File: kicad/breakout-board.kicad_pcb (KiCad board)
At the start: 2 copper layers, 15 parts, among them IC1 ATMEGA328-P, P1 CONN_01X02, P2 Conn_3, P3 Conn_2b, P4 Conn_1, P5 Conn_5, P6 Conn_6, P7 Conn_4, P8 Conn_2b, P9 6Pin Connector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

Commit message: kicad with jumper, flatcam gcode
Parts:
- added JP1: JUMPER, Resistors_ThroughHole:Resistor_Vertical_RM5mm, F.Cu at (28.2, 23.6)
- added JP2: JUMPER, Resistors_ThroughHole:Resistor_Vertical_RM5mm, F.Cu at (38.4, 16.8)
- added JP3: JUMPER, Resistors_ThroughHole:Resistor_Horizontal_RM10mm, F.Cu at (20.8, 16.5)
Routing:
- net +5V: track 46.0 -> 81.3 mm
- net GND: track 2.56 -> 0.00 mm
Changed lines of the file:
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@@
 (kicad_pcb (version 4) (host pcbnew 4.0.0-1rc2.201511201506+6189~38~ubuntu15.04.1-stable)
   (general
-    (links 44)
-    (no_connects 2)
-    (area 0 0 0 0)
+    (links 50)
+    (no_connects 3)
+    (area 11.938 11.390279 55.244 77.884001)
     (thickness 1.6)
-    (drawings 0)
-    (tracks 70)
+    (drawings 2)
+    (tracks 77)
     (zones 0)
-    (modules 15)
+    (modules 18)
     (nets 27)
   )
@@
     (pad_drill 0.6)
     (pad_to_mask_clearance 0)
-    (aux_axis_origin 0 0)
+    (aux_axis_origin 39.624 69.85)
     (visible_elements FFFFFF7F)
     (pcbplotparams
-      (layerselection 0x00030_80000001)
+      (layerselection 0x00000_00000001)
       (usegerberextensions false)
       (excludeedgelayer true)
-      (linewidth 0.100000)
+      (linewidth 0.300000)
       (plotframeref false)
       (viasonmask false)
@@
       (outputformat 1)
       (mirror false)
-      (drillshape 1)
+      (drillshape 0)
       (scaleselection 1)
       (outputdirectory ""))
@@
       (net 4 XTAL2))
   )
-  (segment (start 20.828 18.796) (end 13.97 18.796) (width 0.5) (layer F.Cu) (net 1) (status 400000))
-  (segment (start 14.478 44.45) (end 19.812 44.45) (width 0.5) (layer F.Cu) (net 1) (status 800000))
+  (module Resistors_ThroughHole:Resistor_Vertical_RM5mm (layer F.Cu)
+    (at 28.194 23.622 135)
+    (descr "Resistor, Vertical, RM 5mm, 1/3W,")
+    (tags "Resistor, Vertical, RM 5mm, 1/3W,")
+    (fp_text reference JP1 (at 2.70002 -3.29946 135) (layer F.SilkS)
+      (effects (font (size 1 1) (thickness 0.15)))
+    )
+    (fp_text value JUMPER (at 0 4.50088 135) (layer F.Fab)
+      (effects (font (size 1 1) (thickness 0.15)))
+    )
+    (fp_line (start -0.09906 0) (end 0.9017 0) (layer F.SilkS) (width 0.15))
+    (fp_circle (center -2.49936 0) (end 0 0) (layer F.SilkS) (width 0.15))
+    (pad 1 thru_hole circle (at -2.49936 0 135) (size 1.99898 1.99898) (drill 1.00076) (layers *.Cu *.SilkS *.Mask)
+      (net 2 GND))
+    (pad 2 thru_hole circle (at 2.5019 0 135) (size 1.99898 1.99898) (drill 1.00076) (layers *.Cu *.SilkS *.Mask)
+      (net 2 GND))
+  )
+  (module Resistors_ThroughHole:Resistor_Vertical_RM5mm (layer F.Cu)
+    (at 38.354 16.764 270)
+    (descr "Resistor, Vertical, RM 5mm, 1/3W,")
+    (tags "Resistor, Vertical, RM 5mm, 1/3W,")
+    (fp_text reference JP2 (at 2.70002 -3.29946 270) (layer F.SilkS)
+      (effects (font (size 1 1) (thickness 0.15)))
+    )
+    (fp_text value JUMPER (at 0 4.50088 270) (layer F.Fab)
+      (effects (font (size 1 1) (thickness 0.15)))
+    )
+    (fp_line (start -0.09906 0) (end 0.9017 0) (layer F.SilkS) (width 0.15))
+    (fp_circle (center -2.49936 0) (end 0 0) (layer F.SilkS) (width 0.15))
+    (pad 1 thru_hole circle (at -2.49936 0 180) (size 1.99898 1.99898) (drill 1.00076) (layers *.Cu *.SilkS *.Mask)
+      (net 1 +5V))
+    (pad 2 thru_hole circle (at 2.5019 0 315) (size 1.99898 1.99898) (drill 1.00076) (layers *.Cu *.SilkS *.Mask)
+      (net 1 +5V))
+  )
+  (module Resistors_ThroughHole:Resistor_Horizontal_RM10mm (layer F.Cu)
+    (at 20.828 16.51)
+    (descr "Resistor, Axial,  RM 10mm, 1/3W,")
+    (tags "Resistor, Axial, RM 10mm, 1/3W,")
+    (fp_text reference JP3 (at 0.24892 -3.50012) (layer F.SilkS)
+      (effects (font (size 1 1) (thickness 0.15)))
+    )
+    (fp_text value JUMPER (at 3.81 3.81) (layer F.Fab)
+      (effects (font (size 1 1) (thickness 0.15)))
+    )
+    (fp_line (start -2.54 -1.27) (end 2.54 -1.27) (layer F.SilkS) (width 0.15))
+    (fp_line (start 2.54 -1.27) (end 2.54 1.27) (layer F.SilkS) (width 0.15))
+    (fp_line (start 2.54 1.27) (end -2.54 1.27) (layer F.SilkS) (width 0.15))
+    (fp_line (start -2.54 1.27) (end -2.54 -1.27) (layer F.SilkS) (width 0.15))
+    (fp_line (start -2.54 0) (end -3.81 0) (layer F.SilkS) (width 0.15))
+    (fp_line (start 2.54 0) (end 3.81 0) (layer F.SilkS) (width 0.15))
+    (pad 1 thru_hole circle (at -5.08 0) (size 1.99898 1.99898) (drill 1.00076) (layers *.Cu *.SilkS *.Mask)
+      (net 2 GND))
+    (pad 2 thru_hole circle (at 5.08 0) (size 1.99898 1.99898) (drill 1.00076) (layers *.Cu *.SilkS *.Mask)
+      (net 2 GND))
+    (model Resistors_ThroughHole.3dshapes/Resistor_Horizontal_RM10mm.wrl
+      (at (xyz 0 0 0))
+      (scale (xyz 0.4 0.4 0.4))
+      (rotate (xyz 0 0 0))
+    )
+  )
+  (dimension 59.436 (width 0.3) (layer F.SilkS)
+    (gr_text "59,436 mm" (at 48.594 42.418 270) (layer F.SilkS)
+      (effects (font (size 1.5 1.5) (thickness 0.3)))
+    )
+    (feature1 (pts (xy 42.418 72.136) (xy 49.944 72.136)))
+    (feature2 (pts (xy 42.418 12.7) (xy 49.944 12.7)))
+    (crossbar (pts (xy 47.244 12.7) (xy 47.244 72.136)))
+    (arrow1a (pts (xy 47.244 72.136) (xy 46.657579 71.009496)))
+    (arrow1b (pts (xy 47.244 72.136) (xy 47.830421 71.009496)))
+    (arrow2a (pts (xy 47.244 12.7) (xy 46.657579 13.826504)))
+    (arrow2b (pts (xy 47.244 12.7) (xy 47.830421 13.826504)))
+  )
+  (dimension 30.48 (width 0.3) (layer F.SilkS)
+    (gr_text "30,480 mm" (at 27.178 76.534) (layer F.SilkS)
+      (effects (font (size 1.5 1.5) (thickness 0.3)))
+    )
+    (feature1 (pts (xy 42.418 72.136) (xy 42.418 77.884)))
+    (feature2 (pts (xy 11.938 72.136) (xy 11.938 77.884)))
+    (crossbar (pts (xy 11.938 75.184) (xy 42.418 75.184)))
+    (arrow1a (pts (xy 42.418 75.184) (xy 41.291496 75.770421)))
+    (arrow1b (pts (xy 42.418 75.184) (xy 41.291496 74.597579)))
+    (arrow2a (pts (xy 11.938 75.184) (xy 13.064504 75.770421)))
+    (arrow2b (pts (xy 11.938 75.184) (xy 13.064504 74.597579)))
+  )
+  (segment (start 35.306 18.796) (end 37.8841 18.796) (width 0.5) (layer F.Cu) (net 1))
+  (segment (start 37.8841 18.796) (end 38.354 19.2659) (width 0.5) (layer F.Cu) (net 1))
+  (segment (start 20.828 18.796) (end 20.828 14.986) (width 0.5) (layer F.Cu) (net 1))
+  (segment (start 21.54936 14.26464) (end 38.354 14.26464) (width 0.5) (layer F.Cu) (net 1))
+  (segment (start 20.828 14.986) (end 21.54936 14.26464) (width 0.5) (layer F.Cu) (net 1))
+  (segment (start 37.8841 18.796) (end 38.354 19.2659) (width 0.5) (layer F.Cu) (net 1))
+  (segment (start 22.352 44.45) (end 24.13 44.45) (width 0.5) (layer F.Cu) (net 1))
+  (segment (start 24.13 44.45) (end 29.21 49.53) (width 0.5) (layer F.Cu) (net 1))
+  (segment (start 29.21 49.53) (end 29.972 49.53) (width 0.5) (layer F.Cu) (net 1))
+  (segment (start 20.828 18.796) (end 13.97 18.796) (width 0.5) (layer F.Cu) (net 1))
+  (segment (start 14.478 44.45) (end 19.812 44.45) (width 0.5) (layer F.Cu) (net 1))
   (segment (start 13.716 43.688) (end 14.478 44.45) (width 0.5) (layer F.Cu) (net 1))
   (segment (start 13.716 19.05) (end 13.716 43.688) (width 0.5) (layer F.Cu) (net 1))
   (segment (start 13.97 18.796) (end 13.716 19.05) (width 0.5) (layer F.Cu) (net 1))
-  (segment (start 20.828 18.796) (end 20.828 21.88464) (width 0.5) (layer F.Cu) (net 1) (status 400000))
-  (segment (start 20.828 21.88464) (end 22.31136 23.368) (width 0.5) (layer F.Cu) (net 1) (status 800000))
+  (segment (start 20.828 18.796) (end 20.828 21.88464) (width 0.5) (layer F.Cu) (net 1))
+  (segment (start 20.828 21.88464) (end 22.31136 23.368) (width 0.5) (layer F.Cu) (net 1))
   (segment (start 19.812 44.45) (end 22.352 44.45) (width 0.5) (layer F.Cu) (net 1))
-  (segment (start 19.812 46.95) (end 22.312 46.95) (width 0.5) (layer F.Cu) (net 2))
-  (segment (start 22.312 46.95) (end 22.352 46.99) (width 0.5) (layer F.Cu) (net 2))
   (segment (start 22.352 49.53) (end 17.272 49.53) (width 0.5) (layer F.Cu) (net 3))
   (segment (start 33.274 67.564) (end 28.34894 67.564) (width 0.5) (layer F.Cu) (net 3))
@@
   (segment (start 18.756 67.564) (end 23.46706 67.564) (width 0.5) (layer F.Cu) (net 4))
   (segment (start 17.272 52.07) (end 22.352 52.07) (width 0.5) (layer F.Cu) (net 4))
-  (segment (start 17.3101 23.368) (end 17.3101 29.1719) (width 0.5) (layer F.Cu) (net 5) (status C00000))
-  (segment (start 17.3101 29.1719) (end 17.272 29.21) (width 0.5) (layer F.Cu) (net 5) (status C00000))
+  (segment (start 17.3101 23.368) (end 17.3101 29.1719) (width 0.5) (layer F.Cu) (net 5))
+  (segment (start 17.3101 29.1719) (end 17.272 29.21) (width 0.5) (layer F.Cu) (net 5))
   (segment (start 17.3101 24.13) (end 17.3101 23.9141) (width 0.5) (layer F.Cu) (net 5))
   (segment (start 22.352 29.21) (end 30.226 21.336) (width 0.5) (layer F.Cu) (net 5))

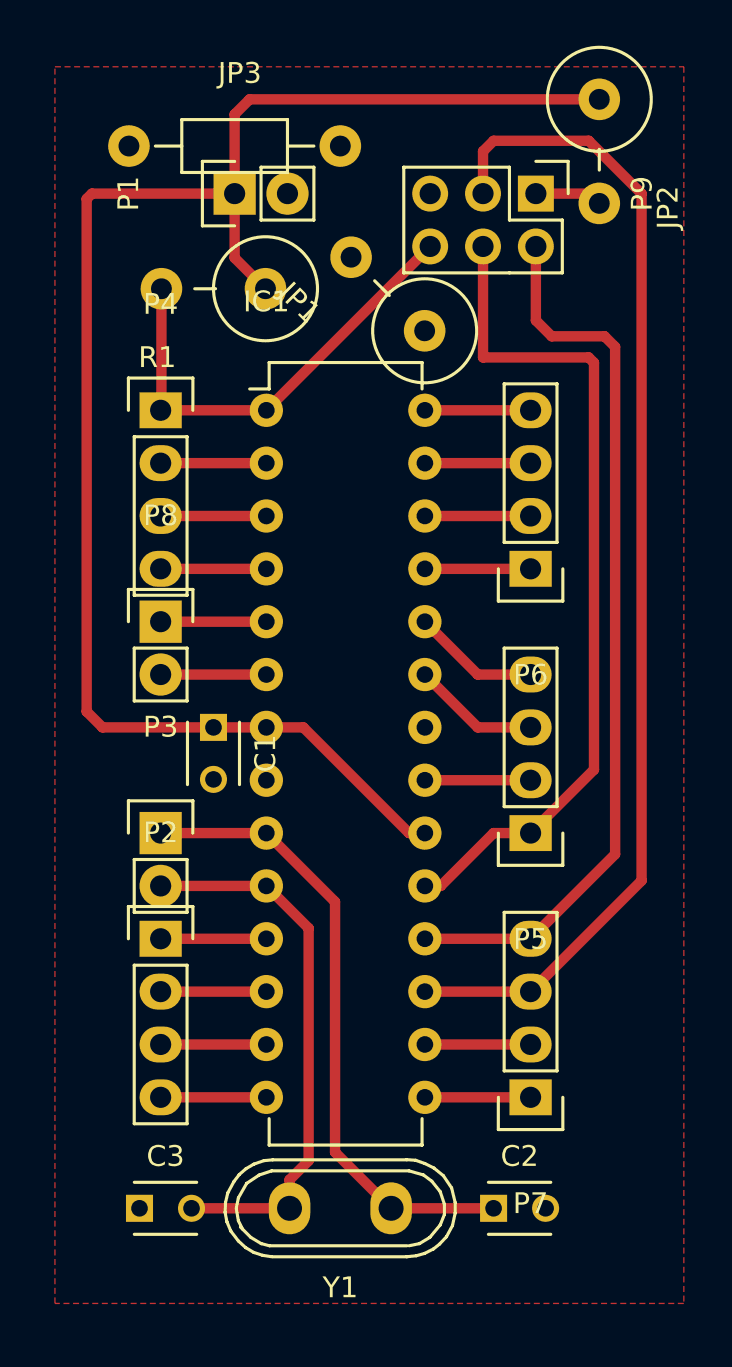
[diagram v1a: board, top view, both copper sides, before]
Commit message: redesign fully header connected
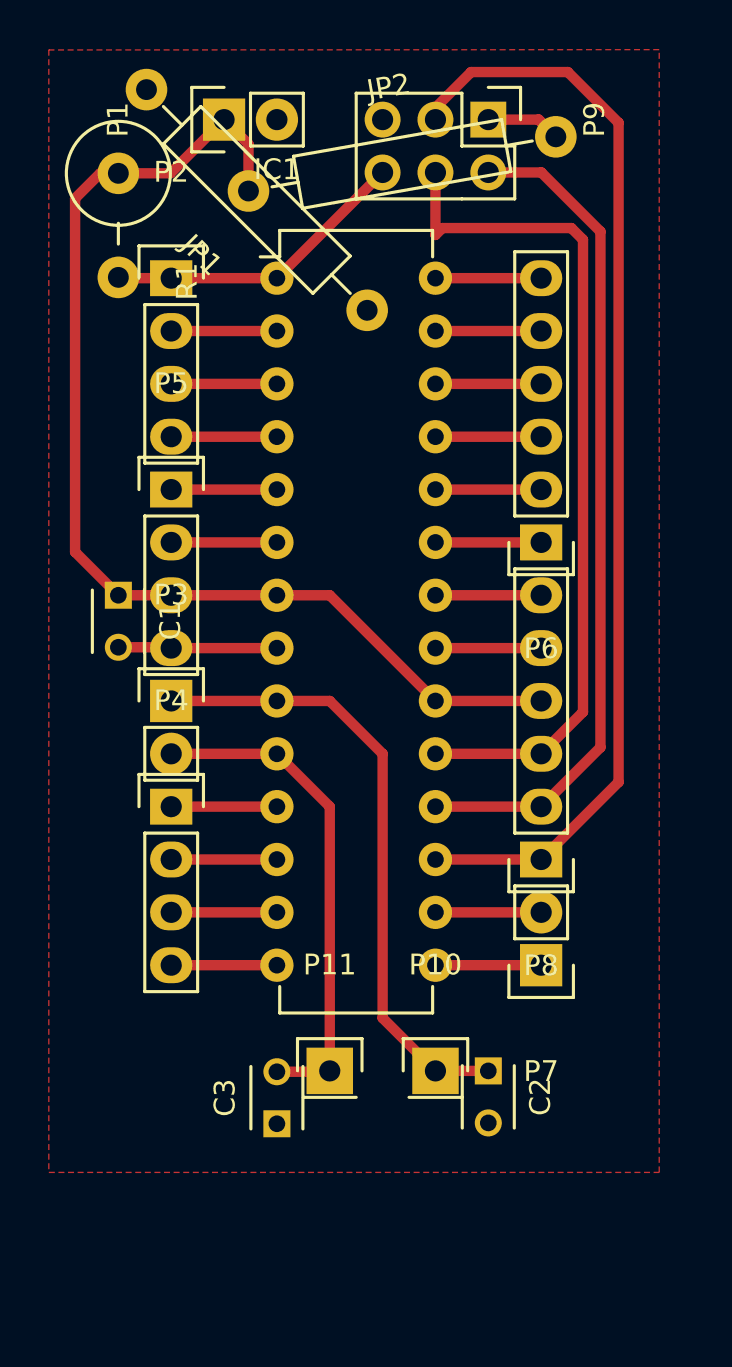
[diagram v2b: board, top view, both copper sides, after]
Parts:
- removed JP3: JUMPER, Resistors_ThroughHole:Resistor_Horizontal_RM10mm
- removed Y1: 16MHz, Crystals:Crystal_HC50-U_Vertical
- added P10: CONN_01X01, Pin_Headers:Pin_Header_Straight_1x01, F.Cu at (30.5, 61.0)
- added P11: CONN_01X01, Pin_Headers:Pin_Header_Straight_1x01, F.Cu at (25.4, 61.0)
- JP1, JP2: footprint Resistors_ThroughHole:Resistor_Vertical_RM5mm -> Resistors_ThroughHole:Resistor_Horizontal_RM15mm
- P2: value Conn_3 -> CONN_01X04
- P3: value Conn_2b -> CONN_01X02
- P4: value Conn_1 -> CONN_01X04
- P5: value Conn_5 -> CONN_01X04
- P6: value Conn_6 -> CONN_01X06; footprint Pin_Headers:Pin_Header_Straight_1x04 -> Pin_Headers:Pin_Header_Straight_1x06
- P7: value Conn_4 -> CONN_01X02; footprint Pin_Headers:Pin_Header_Straight_1x04 -> Pin_Headers:Pin_Header_Straight_1x02
- P8: value Conn_2b -> CONN_01X06; footprint Pin_Headers:Pin_Header_Straight_1x02 -> Pin_Headers:Pin_Header_Straight_1x06
- moved P2 31.8 mm to (17.8, 22.9)
- moved P5 23.9 mm to (17.8, 33.0), turned to 0 degrees
- moved P8 21.6 mm to (35.6, 50.8), turned to 180 degrees
- moved P4 19.1 mm to (17.8, 48.3)
- moved JP2 9.49 mm to (28.9, 17.4), turned to 10 degrees
- moved C1 7.82 mm to (15.2, 38.1)
- moved C3 7.75 mm to (22.9, 63.5), turned to 90 degrees
- moved JP1 7.75 mm to (21.9, 19.1)
- moved C2 6.61 mm to (33.0, 61.0), turned to 270 degrees
- moved IC1 6.37 mm to (22.9, 22.9)
- moved P3 6.37 mm to (17.8, 43.2)
- moved P7 6.37 mm to (35.6, 55.9)
- moved R1 5.49 mm to (15.2, 20.3), turned to 270 degrees
- moved P9 4.23 mm to (33.0, 15.2)
- moved P1 3.59 mm to (20.3, 15.2)
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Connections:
- P2 pad 1: PD5 -> RESET
- P2 pad 2: PD6 -> PD0
- P2 pad 3: PD7 -> PD1
- P2 pad 4: PB0 -> PD2
- P4 pad 1: RESET -> PD5
- P4 pad 2: PD0 -> PD6
- P4 pad 3: PD1 -> PD7
- P4 pad 4: PD2 -> PB0
- P5 pad 1: SCK -> PD3
- P5 pad 2: AREF -> PD4
- P5 pad 3: PC0 -> +5V
- P5 pad 4: PC1 -> GND
- P6 pad 1: PC2 -> PC0
- P6 pad 2: PC3 -> PC1
- P6 pad 3: PC4 -> PC2
- P6 pad 4: PC5 -> PC3
- P8 pad 1: PD3 -> MOSI
- P8 pad 2: PD4 -> MISO
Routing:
- net +5V: track 81.3 -> 59.8 mm
- net GND: track 0.00 -> 12.7 mm
- net RESET: track 22.3 -> 14.8 mm
- net MOSI: track 57.1 -> 53.1 mm
- net MISO: track 43.1 -> 40.5 mm
- net XTAL2: track 26.5 -> 23.9 mm
- net PC0: track 6.13 -> 5.08 mm
- net PC1: track 6.13 -> 5.08 mm

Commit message: redesign mirror and re-place isp, make it smaller
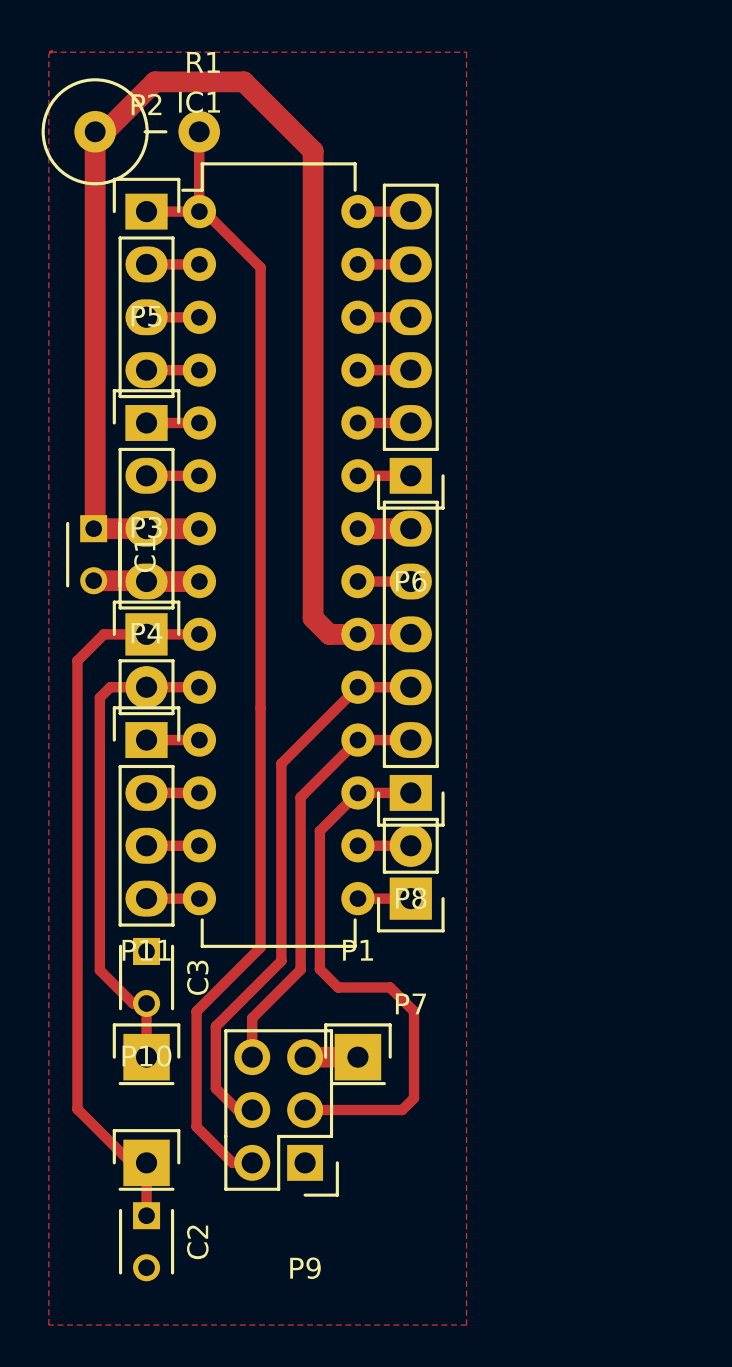
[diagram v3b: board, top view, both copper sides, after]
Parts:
- removed JP1, JP2: JUMPER, Resistors_ThroughHole:Resistor_Horizontal_RM15mm
- P1: value CONN_01X02 -> CONN_01X01; footprint Pin_Headers:Pin_Header_Straight_1x02 -> Pin_Headers:Pin_Header_Straight_1x01
- moved P9 50.9 mm to (24.2, 65.4), turned to 180 degrees
- moved P1 45.5 mm to (26.8, 60.3), turned to 0 degrees
- moved C2 17.8 mm to (16.6, 67.9)
- moved P10 14.6 mm to (16.6, 65.4)
- moved C3 10.4 mm to (16.6, 55.2), turned to 270 degrees
- moved P11 8.83 mm to (16.6, 60.3)
- moved P6 7.03 mm to (29.3, 32.4)
- moved P7 7.03 mm to (29.3, 52.7)
- moved P8 7.03 mm to (29.3, 47.6)
- moved IC1 4.91 mm to (19.1, 19.7)
- moved R1 4.70 mm to (16.6, 15.8), turned to 0 degrees
- moved P3 3.41 mm to (16.6, 40.0)
- moved P5 3.41 mm to (16.6, 29.8)
- moved C1 3.41 mm to (14.1, 34.9)
- moved P2 3.41 mm to (16.6, 19.7)
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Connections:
- P9 pad 1: +5V -> GND
- P9 pad 2: MISO -> RESET
- P9 pad 5: GND -> +5V
- P9 pad 6: RESET -> MISO
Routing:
- net RESET: track 14.8 -> 57.1 mm
- net MOSI: track 53.1 -> 26.8 mm
- net MISO: track 40.5 -> 19.9 mm
- net SCK: track 41.1 -> 27.5 mm
- net +5V: track 59.8 -> 67.0 mm
- net GND: track 12.7 -> 7.69 mm
- net XTAL1: track 30.0 -> 34.9 mm
- net PC5: track 5.08 -> 2.54 mm
- net PC4: track 5.08 -> 2.54 mm
- net PC3: track 5.08 -> 2.54 mm
- net PC2: track 5.08 -> 2.54 mm
- net PC1: track 5.08 -> 2.54 mm
- net PC0: track 5.08 -> 2.54 mm
- net PB2: track 5.08 -> 2.54 mm
- net PB1: track 5.08 -> 2.54 mm
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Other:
- net class Power added: clearance 0.3, trace_width 1, via_dia 0.6, via_drill 0.4
